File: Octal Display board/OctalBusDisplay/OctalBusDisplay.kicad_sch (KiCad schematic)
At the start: 18 parts, among them IC1 TIL311, IC10 TIL311, IC11 TIL311, IC12 TIL311, IC13 TIL311, IC14 TIL311, IC2 TIL311, IC3 TIL311, IC4 TIL311, IC5 TIL311, IC6 TIL311, IC7 TIL311, IC8 TIL311, IC9 TIL311, J1 86093967113745ELF, U1 74AHC1G08

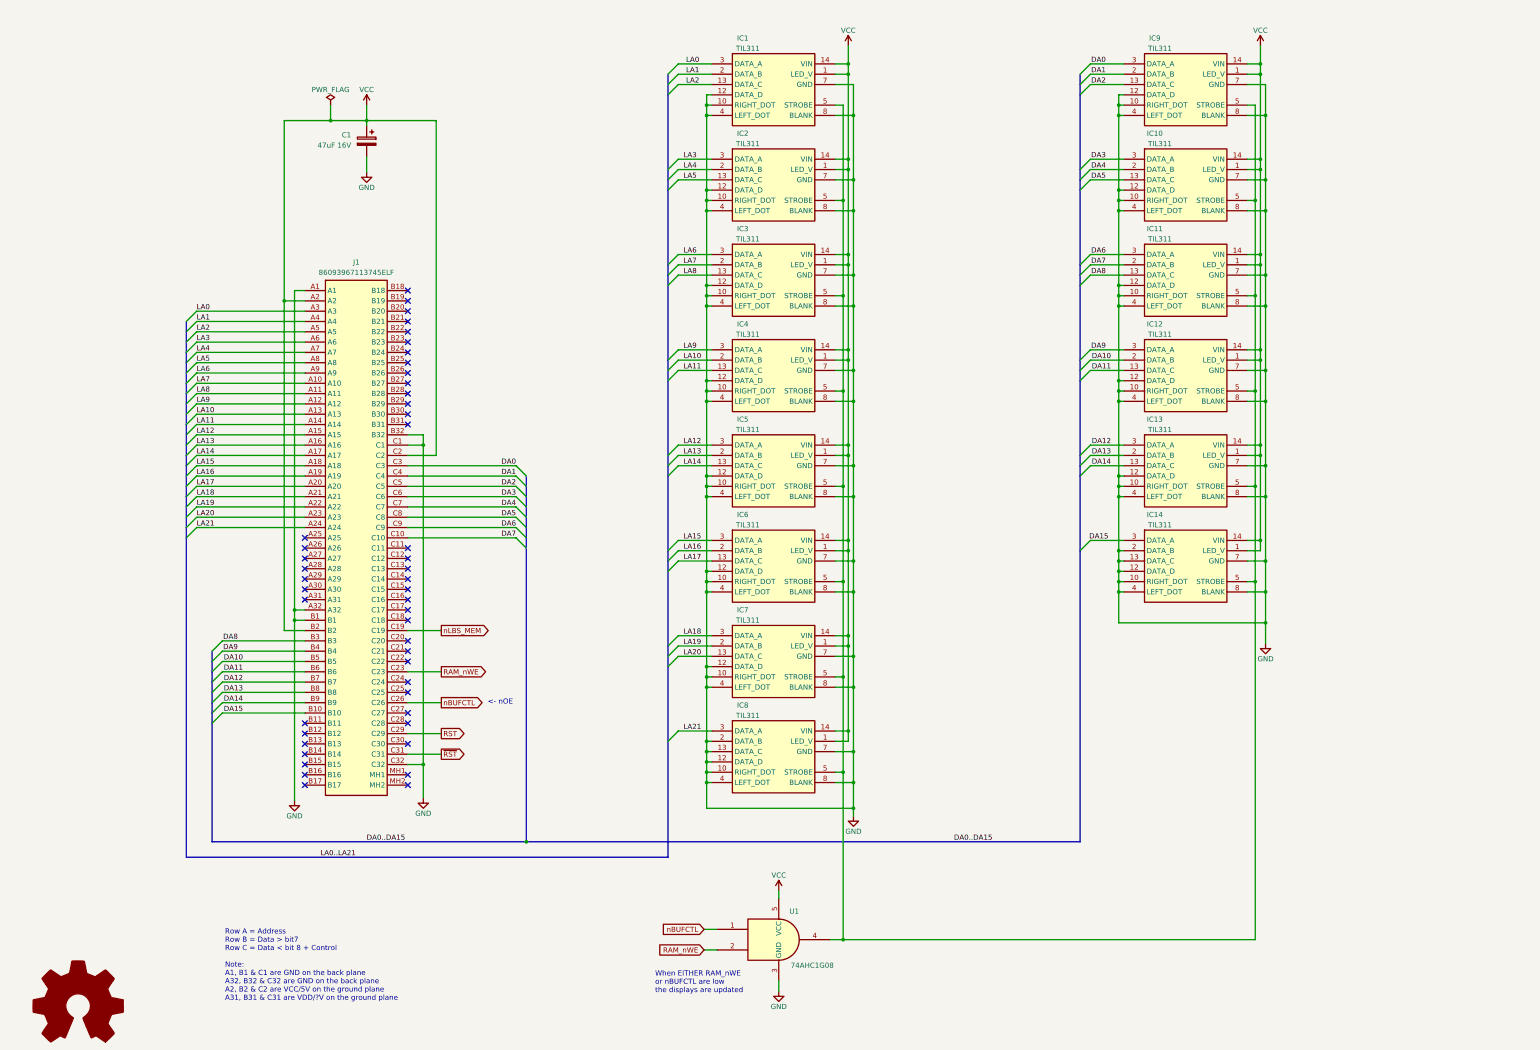
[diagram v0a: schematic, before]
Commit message: Added 16x16 dotmatrix display PCB and test code
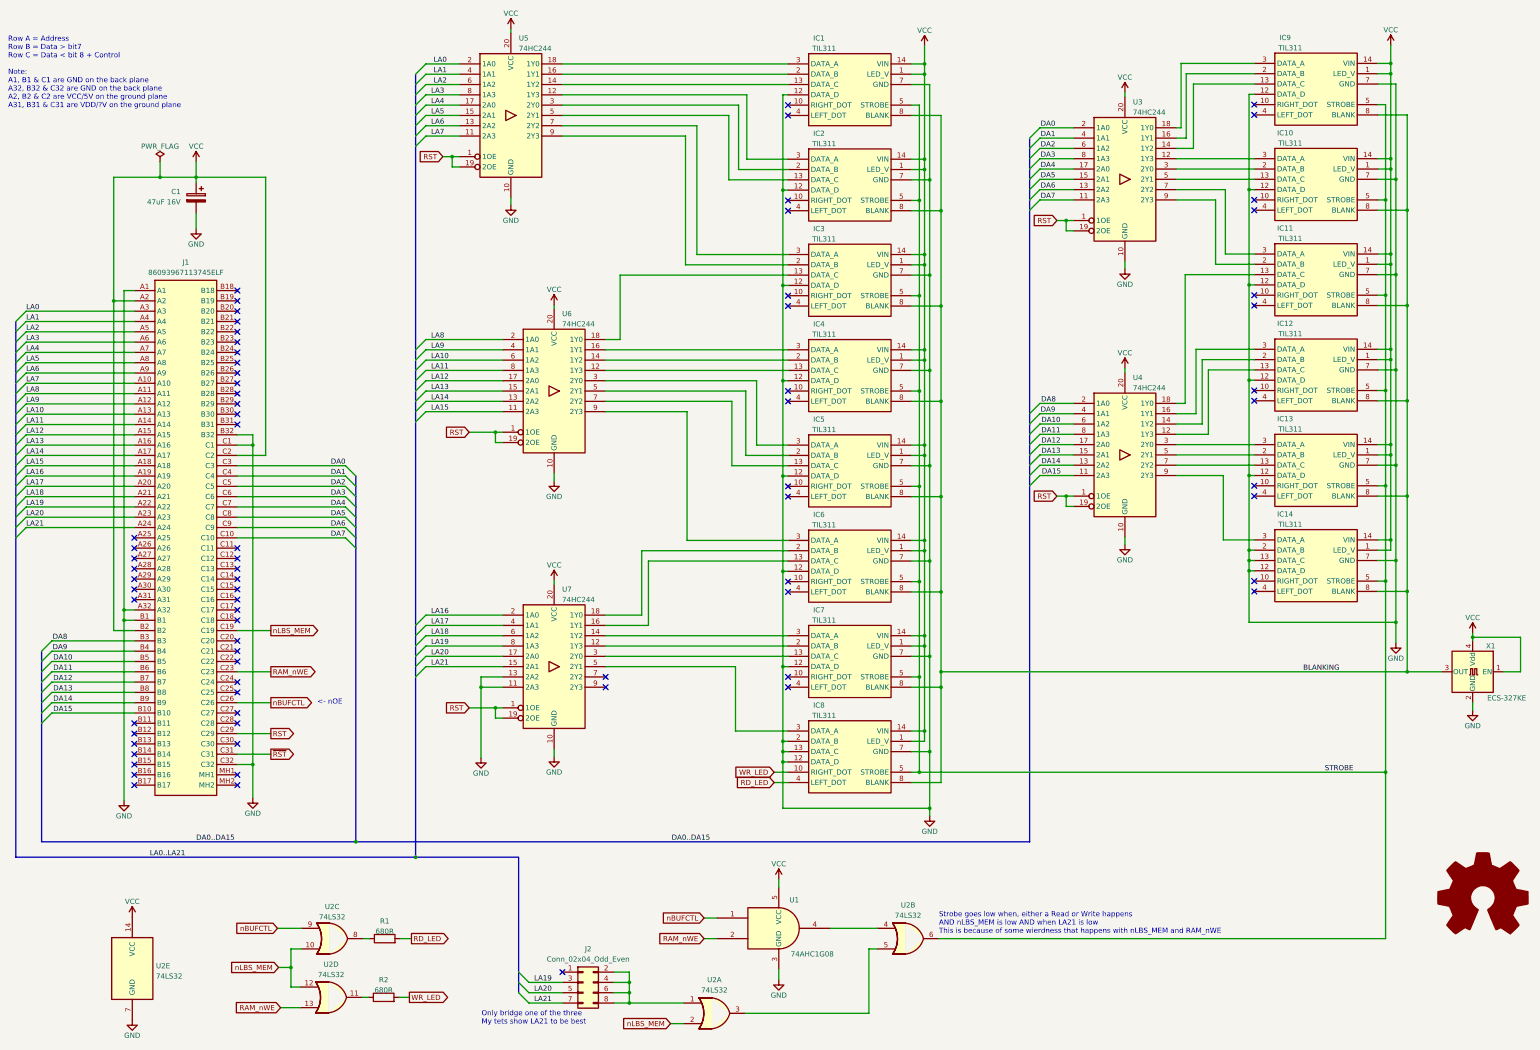
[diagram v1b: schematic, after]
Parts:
- added J2: Conn_02x04_Odd_Even, Package_SO:SSOP-8_2.95x2.8mm_P0.65mm, symbol Connector_Generic:Conn_02x04_Odd_Even
- added R1, R2: 680R, Resistor_SMD:R_0603_1608Metric, symbol Device:R
- added U2: 74LS32, Package_SO:SOIC-14_3.9x8.7mm_P1.27mm, symbol 74xx:74LS32
- added U3, U4, U5, U6, U7: 74HC244, Package_SO:SOIC-20W_7.5x12.8mm_P1.27mm, symbol 74xx:74HC244
- added X1: ECS-327KE, Oscillator:Oscillator_SMD_Abracon_ASE-4Pin_3.2x2.5mm, symbol Oscillator:ASE-xxxMHz
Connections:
- net DA0: now also U3.2 (1A0); no longer IC9.3 (DATA_A)
- net DA1: now also U3.4 (1A1); no longer IC9.2 (DATA_B)
- net DA10: now also U4.6 (1A2); no longer IC12.2 (DATA_B)
- net DA11: now also U4.8 (1A3); no longer IC12.13 (DATA_C)
- net DA12: now also U4.17 (2A0); no longer IC13.3 (DATA_A)
- net DA13: now also U4.15 (2A1); no longer IC13.2 (DATA_B)
- net DA14: now also U4.13 (2A2); no longer IC13.13 (DATA_C)
- net DA15: now also U4.11 (2A3); no longer IC14.3 (DATA_A)
- net DA2: now also U3.6 (1A2); no longer IC9.13 (DATA_C)
- net DA3: now also U3.8 (1A3); no longer IC10.3 (DATA_A)
- net DA4: now also U3.17 (2A0); no longer IC10.2 (DATA_B)
- net DA5: now also U3.15 (2A1); no longer IC10.13 (DATA_C)
- net DA6: now also U3.13 (2A2); no longer IC11.3 (DATA_A)
- net DA7: now also U3.11 (2A3); no longer IC11.2 (DATA_B)
- net DA8: now also U4.2 (1A0); no longer IC11.13 (DATA_C)
- net DA9: now also U4.4 (1A1); no longer IC12.3 (DATA_A)
- net GND: now also U2.7 (GND), U3.10 (GND), U4.10 (GND), U5.10 (GND), U6.10 (GND), U7.10 (GND), U7.11 (2A3), U7.13 (2A2), X1.2 (GND); no longer IC1.10 (RIGHT_DOT), IC1.4 (LEFT_DOT), IC1.8 (BLANK), IC10.10 (RIGHT_DOT), IC10.4 (LEFT_DOT), IC10.8 (BLANK), IC11.10 (RIGHT_DOT), IC11.4 (LEFT_DOT), IC11.8 (BLANK), IC12.10 (RIGHT_DOT), IC12.4 (LEFT_DOT), IC12.8 (BLANK), IC13.10 (RIGHT_DOT), IC13.4 (LEFT_DOT), IC13.8 (BLANK), IC14.10 (RIGHT_DOT), IC14.4 (LEFT_DOT), IC14.8 (BLANK), IC2.10 (RIGHT_DOT), IC2.4 (LEFT_DOT), IC2.8 (BLANK), IC3.10 (RIGHT_DOT), IC3.4 (LEFT_DOT), IC3.8 (BLANK), IC4.10 (RIGHT_DOT), IC4.4 (LEFT_DOT), IC4.8 (BLANK), IC5.10 (RIGHT_DOT), IC5.4 (LEFT_DOT), IC5.8 (BLANK), IC6.10 (RIGHT_DOT), IC6.4 (LEFT_DOT), IC6.8 (BLANK), IC7.10 (RIGHT_DOT), IC7.4 (LEFT_DOT), IC7.8 (BLANK), IC8.10 (RIGHT_DOT), IC8.4 (LEFT_DOT), IC8.8 (BLANK), IC9.10 (RIGHT_DOT), IC9.4 (LEFT_DOT), IC9.8 (BLANK)
- net LA0: now also U5.2 (1A0); no longer IC1.3 (DATA_A)
- net LA1: now also U5.4 (1A1); no longer IC1.2 (DATA_B)
- net LA10: now also U6.6 (1A2); no longer IC4.2 (DATA_B)
- net LA11: now also U6.8 (1A3); no longer IC4.13 (DATA_C)
- net LA12: now also U6.17 (2A0); no longer IC5.3 (DATA_A)
- net LA13: now also U6.15 (2A1); no longer IC5.2 (DATA_B)
- net LA14: now also U6.13 (2A2); no longer IC5.13 (DATA_C)
- net LA15: now also U6.11 (2A3); no longer IC6.3 (DATA_A)
- net LA16: now also U7.2 (1A0); no longer IC6.2 (DATA_B)
- net LA17: now also U7.4 (1A1); no longer IC6.13 (DATA_C)
- net LA18: now also U7.6 (1A2); no longer IC7.3 (DATA_A)
- net LA19: now also J2.3 (Pin_3), U7.8 (1A3); no longer IC7.2 (DATA_B)
- net LA2: now also U5.6 (1A2); no longer IC1.13 (DATA_C)
- net LA20: now also J2.5 (Pin_5), U7.17 (2A0); no longer IC7.13 (DATA_C)
- net LA21: now also J2.7 (Pin_7), U7.15 (2A1); no longer IC8.3 (DATA_A)
- net LA3: now also U5.8 (1A3); no longer IC2.3 (DATA_A)
- net LA4: now also U5.17 (2A0); no longer IC2.2 (DATA_B)
- net LA5: now also U5.15 (2A1); no longer IC2.13 (DATA_C)
- net LA6: now also U5.13 (2A2); no longer IC3.3 (DATA_A)
- net LA7: now also U5.11 (2A3); no longer IC3.2 (DATA_B)
- net LA8: now also U6.2 (1A0); no longer IC3.13 (DATA_C)
- net LA9: now also U6.4 (1A1); no longer IC4.3 (DATA_A)
- net RAM_nWE: now also U2.13
- net RST: now also U3.1 (1OE), U3.19 (2OE), U4.1 (1OE), U4.19 (2OE), U5.1 (1OE), U5.19 (2OE), U6.1 (1OE), U6.19 (2OE), U7.1 (1OE), U7.19 (2OE)
- net VCC: now also U2.14 (VCC), U3.20 (VCC), U4.20 (VCC), U5.20 (VCC), U6.20 (VCC), U7.20 (VCC), X1.1 (EN), X1.4 (Vdd)
- net nBUFCTL: now also U2.9
- net nLBS_MEM: now also U2.10, U2.12, U2.2
- net STROBE: now reaches IC1.5 (STROBE), IC10.5 (STROBE), IC11.5 (STROBE), IC12.5 (STROBE), IC13.5 (STROBE), IC14.5 (STROBE), IC2.5 (STROBE), IC3.5 (STROBE), IC4.5 (STROBE), IC5.5 (STROBE), IC6.5 (STROBE), IC7.5 (STROBE), IC8.5 (STROBE), IC9.5 (STROBE)
- net STROBE: now also U2.6; no longer U1.4
- new net: U1.4, U2.4
- new net: U2.3, U2.5
- new net: J2.2 (Pin_2), J2.4 (Pin_4), J2.6 (Pin_6), J2.8 (Pin_8), U2.1
- new net: IC7.13 (DATA_C), U7.3 (2Y0)
- new net: IC7.2 (DATA_B), U7.12 (1Y3)
- new net: IC7.3 (DATA_A), U7.14 (1Y2)
- new net: R2.1, U2.11
- new net: R1.1, U2.8
- new net: IC6.13 (DATA_C), U7.16 (1Y1)
- new net: IC6.2 (DATA_B), U7.18 (1Y0)
- new net: IC8.3 (DATA_A), U7.5 (2Y1)
- new net: IC6.3 (DATA_A), U6.9 (2Y3)
- new net: IC1.13 (DATA_C), U5.14 (1Y2)
- new net: IC1.2 (DATA_B), U5.16 (1Y1)
- new net: IC1.3 (DATA_A), U5.18 (1Y0)
- new net: IC13.13 (DATA_C), U4.7 (2Y2)
- new net: IC13.2 (DATA_B), U4.5 (2Y1)
- new net: IC13.3 (DATA_A), U4.3 (2Y0)
- new net: IC2.13 (DATA_C), U5.5 (2Y1)
- new net: IC2.2 (DATA_B), U5.3 (2Y0)
- new net: IC2.3 (DATA_A), U5.12 (1Y3)
- new net: IC4.13 (DATA_C), U6.12 (1Y3)
- new net: IC4.2 (DATA_B), U6.14 (1Y2)
- new net: IC4.3 (DATA_A), U6.16 (1Y1)
- new net: IC3.3 (DATA_A), U5.7 (2Y2)
- new net: IC3.2 (DATA_B), U5.9 (2Y3)
- new net: IC3.13 (DATA_C), U6.18 (1Y0)
- new net: IC14.3 (DATA_A), U4.9 (2Y3)
- new net: IC11.13 (DATA_C), U4.18 (1Y0)
- new net: IC11.2 (DATA_B), U3.9 (2Y3)
- new net: IC11.3 (DATA_A), U3.7 (2Y2)
- new net: IC12.13 (DATA_C), U4.12 (1Y3)
- new net: IC12.2 (DATA_B), U4.14 (1Y2)
- new net: IC12.3 (DATA_A), U4.16 (1Y1)
- new net: IC9.13 (DATA_C), U3.14 (1Y2)
- new net: IC9.2 (DATA_B), U3.16 (1Y1)
- new net: IC9.3 (DATA_A), U3.18 (1Y0)
- new net: IC10.13 (DATA_C), U3.5 (2Y1)
- new net: IC10.2 (DATA_B), U3.3 (2Y0)
- new net: IC10.3 (DATA_A), U3.12 (1Y3)
- new net: IC5.3 (DATA_A), U6.3 (2Y0)
- new net: IC5.2 (DATA_B), U6.5 (2Y1)
- new net: IC5.13 (DATA_C), U6.7 (2Y2)
- new net BLANKING: IC1.8 (BLANK), IC10.8 (BLANK), IC11.8 (BLANK), IC12.8 (BLANK), IC13.8 (BLANK), IC14.8 (BLANK), IC2.8 (BLANK), IC3.8 (BLANK), IC4.8 (BLANK), IC5.8 (BLANK), IC6.8 (BLANK), IC7.8 (BLANK), IC8.8 (BLANK), IC9.8 (BLANK), X1.3 (OUT)
- new net RD_LED: IC8.4 (LEFT_DOT), R1.2
- new net WR_LED: IC8.10 (RIGHT_DOT), R2.2
- no-connect marks 46 -> 75
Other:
- note added: "Only bridge one of the three My tets show LA21 to be best"
- note added: "Strobe goes low when, either a Read or Write happens AND nLBS_MEM is low AND when LA21 is low This is because of some wierdness that happens with nLBS_MEM and RAM_nWE"
- note removed: "When EITHER RAM_nWE or nBUFCTL are low the displays are updated"
- moved on the sheet: C1, IC1, IC10, IC11, IC12, IC13, IC14, IC2, IC3, IC4, IC5, IC6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
